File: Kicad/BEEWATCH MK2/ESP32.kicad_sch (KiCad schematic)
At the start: 42 parts, among them J1 USB_C_Receptacle_USB2.0, Q1 DMG6968U, SW1 TK-074-4, SW2 TK-074-4, U1 ESP32-S3FH4R2, Y1 40MHz, Y2 32.768KHz

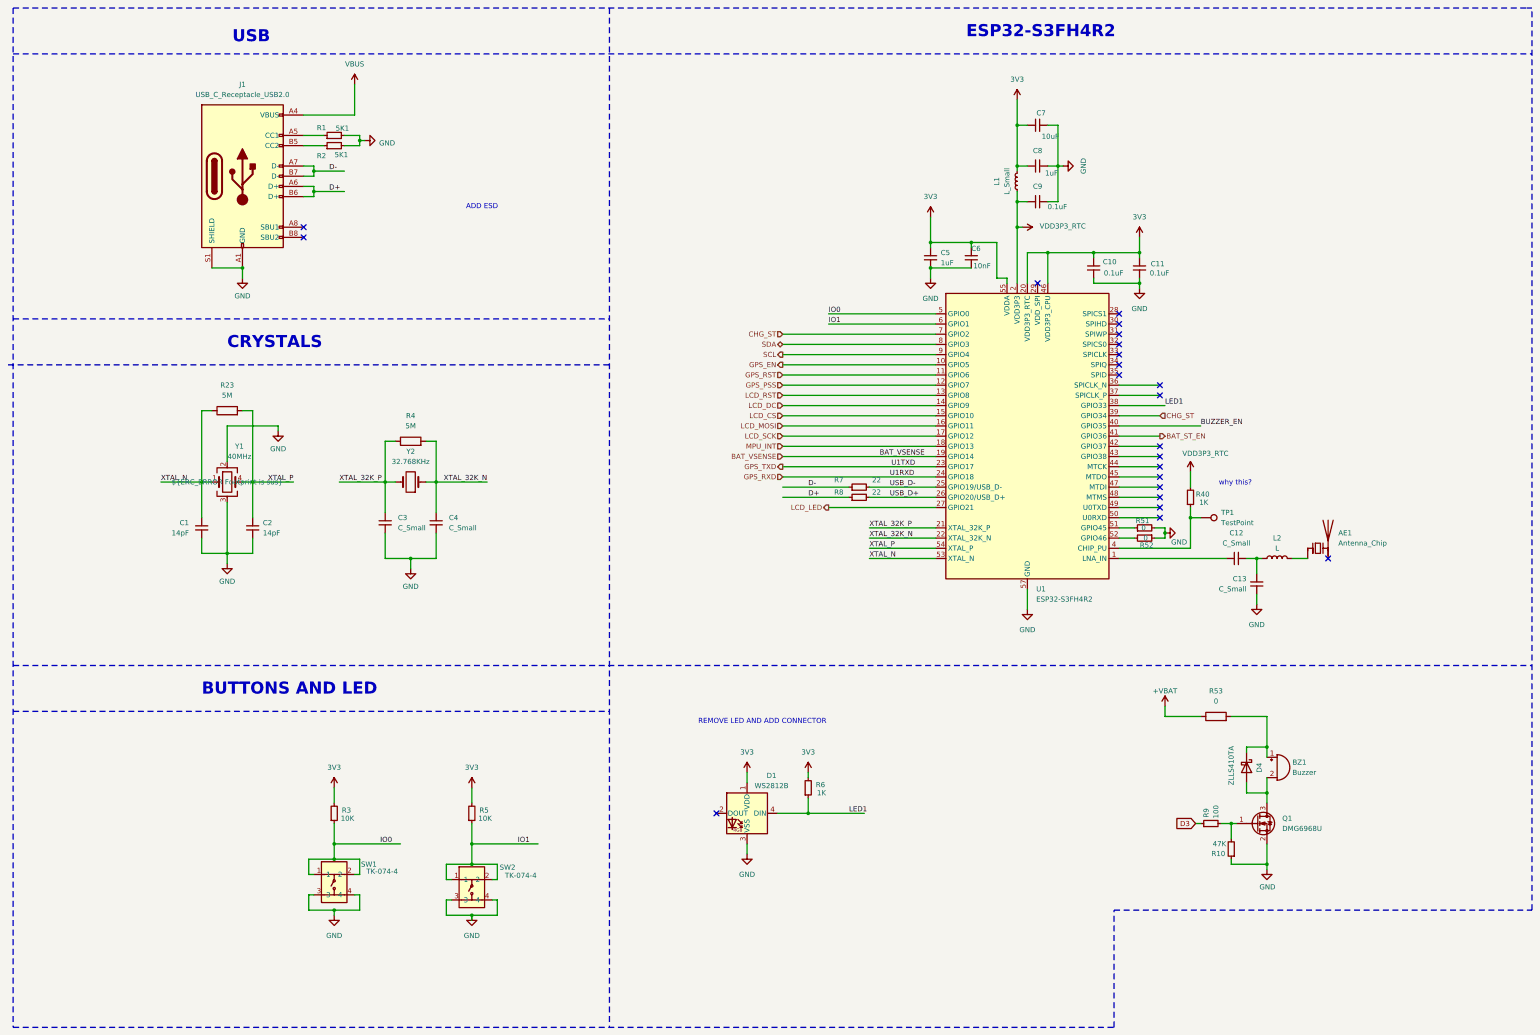
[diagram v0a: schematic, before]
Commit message: ERC going on anf All Lib issue is fixed
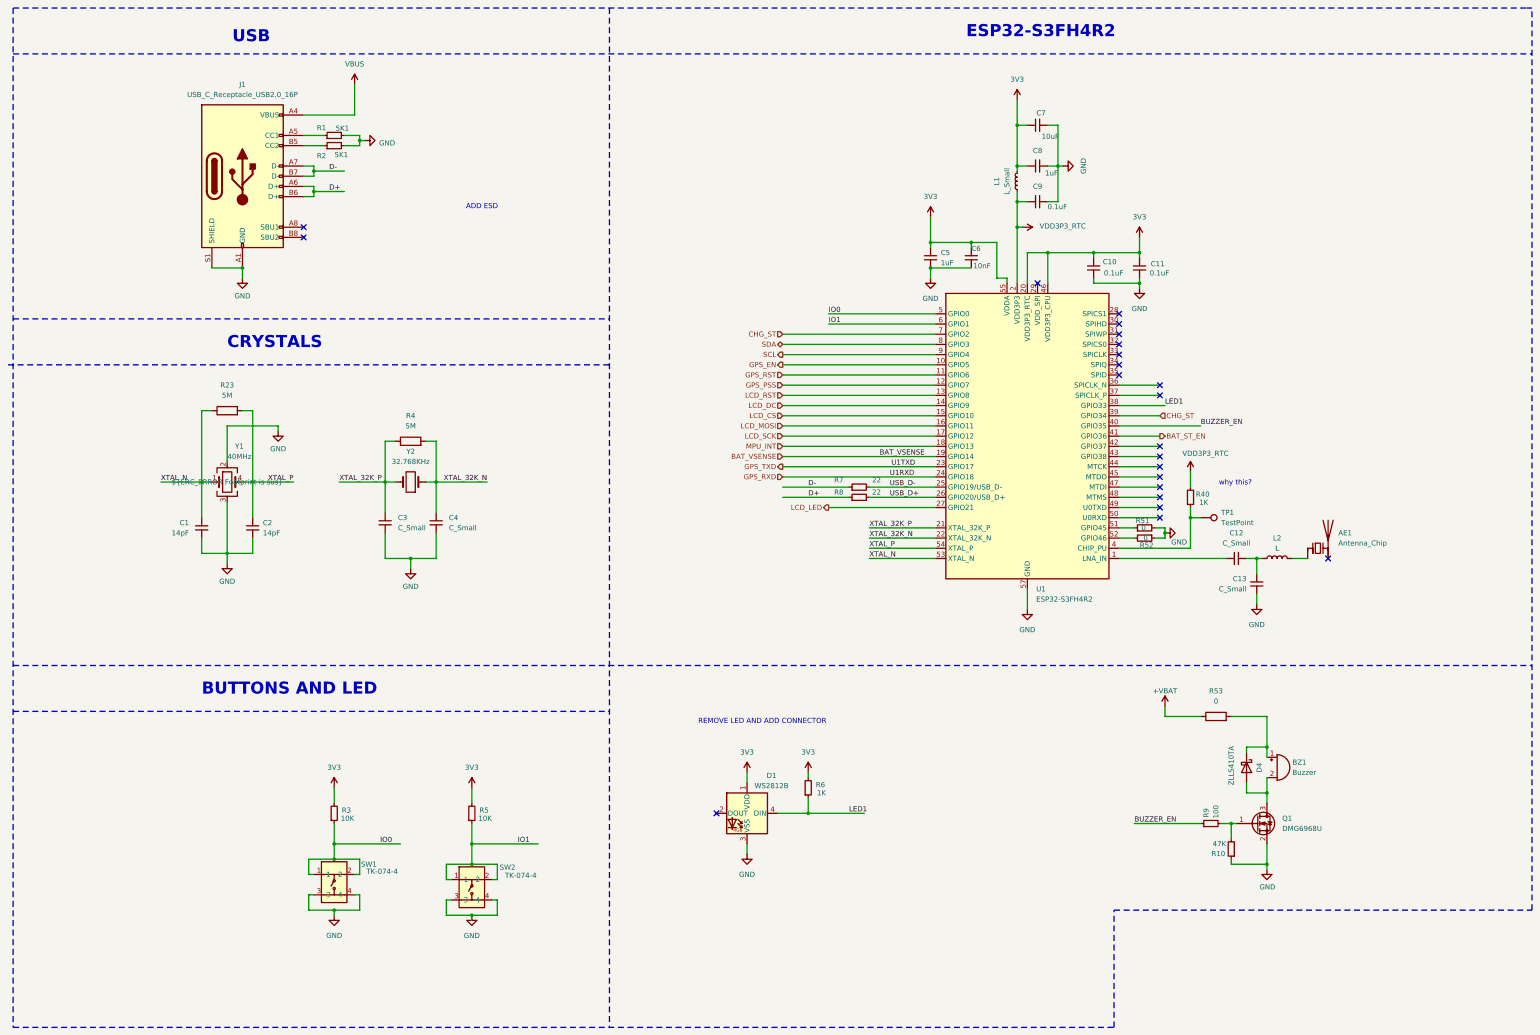
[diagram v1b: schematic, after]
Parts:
- removed J1: USB_C_Receptacle_USB2.0, Connector_USB:USB_C_Receptacle_G-Switch_GT-USB-7010ASV, symbol Connector:USB_C_Receptacle_USB2.0
- added J1: USB_C_Receptacle_USB2.0_16P, symbol Connector:USB_C_Receptacle_USB2.0_16P
- D1: footprint SM_LED:XL-0807RGBC-WS2812B -> LED_SMD:LED_WS2812B_PLCC4_5.0x5.0mm_P3.2mm
- SW1, SW2: footprint SM_SWITCH:Tact Switch-TK-074-4 Pin SMD -> Project:Tact Switch-TK-074-4 Pin SMD
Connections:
- net D3 is gone; now on net BUZZER_EN: R9.1
- net D+: now also J1.A6 (D+), J1.B6 (D+)
- net D-: now also J1.A7 (D-), J1.B7 (D-)
- net GND: now also J1.A1 (GND), J1.A12 (GND), J1.B1 (GND), J1.B12 (GND), J1.S1 (SHIELD)
- net VBUS: now also J1.A4 (VBUS), J1.A9 (VBUS), J1.B4 (VBUS), J1.B9 (VBUS)
- net at R1.1: now also J1.A5 (CC1)
- net at R2.1: now also J1.B5 (CC2)
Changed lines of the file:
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@@
 	)
 	(junction
-		(at 77.47 86.36)
-		(diameter 0)
-		(color 0 0 0 0)
-	)
-	(junction
 		(at 323.85 224.79)
 		(diameter 0)
@@
 	)
 	(junction
+		(at 77.47 86.36)
+		(diameter 0)
+		(color 0 0 0 0)
+	)
+	(junction
 		(at 248.92 86.36)
 		(diameter 0)
@@
 	(wire
 		(pts
-			(xy 314.96 224.79) (xy 316.23 224.79)
+			(xy 299.72 224.79) (xy 316.23 224.79)
 		)
 		(stroke
@@
 		)
 	)
+	(label "BUZZER_EN"
+		(at 299.72 224.79 0)
+		(effects
+			(font
+				(size 1.27 1.27)
+			)
+			(justify left bottom)
+		)
+	)
 	(label "U1TXD"
 		(at 245.11 135.89 180)
@@
 		)
 	)
-	(global_label "D3"
-		(shape input)
-		(at 314.96 224.79 180)
-		(effects
-			(font
-				(size 1.27 1.27)
-			)
-			(justify right)
-		)
-		(property "Intersheetrefs" "${INTERSHEET_REFS}"
-			(at 314.96 224.79 0)
-			(effects
-				(font
-					(size 1.27 1.27)
-				)
-				(hide yes)
-			)
-		)
-	)
 	(hierarchical_label "GPS_RXD"
 		(shape input)
@@
 	)
 	(symbol
-		(lib_id "Connector:USB_C_Receptacle_USB2.0")
-		(at 77.47 63.5 0)
-		(unit 1)
-		(exclude_from_sim no)
-		(in_bom yes)
-		(on_board yes)
-		(dnp no)
-		(fields_autoplaced yes)
-		(property "Reference" "J1"
-			(at 77.47 40.64 0)
-			(effects
-				(font
-					(size 1.27 1.27)
-				)
-			)
-		)
-		(property "Value" "USB_C_Receptacle_USB2.0"
-			(at 77.47 43.18 0)
-			(effects
-				(font
-					(size 1.27 1.27)
-				)
-			)
-		)
-		(property "Footprint" "Connector_USB:USB_C_Receptacle_G-Switch_GT-USB-7010ASV"
-			(at 81.28 63.5 0)
-			(effects
-				(font
-					(size 1.27 1.27)
-				)
-				(hide yes)
-			)
-		)
-		(property "Datasheet" "https://www.usb.org/sites/default/files/documents/usb_type-c.zip"
-			(at 81.28 63.5 0)
-			(effects
-				(font
-					(size 1.27 1.27)
-				)
-				(hide yes)
-			)
-		)
-		(property "Description" ""
-			(at 77.47 63.5 0)
-			(effects
-				(font
-					(size 1.27 1.27)
-				)
-				(hide yes)
-			)
-		)
-		(pin "A1"
-		)
-		(pin "A12"
-		)
-		(pin "A4"
-		)
-		(pin "A5"
-		)
-		(pin "A6"
-		)
-		(pin "A7"
-		)
-		(pin "A8"
-		)
-		(pin "A9"
-		)
-		(pin "B1"
-		)
-		(pin "B12"
-		)
-		(pin "B4"
-		)
-		(pin "B5"
-		)
-		(pin "B6"
-		)
-		(pin "B7"
-		)
-		(pin "B8"
-		)
-		(pin "B9"
-		)
-		(pin "S1"
-		)
-		(instances
-			(project "BEEWATCH"
-				(path "/e9c5fb53-480b-4989-8495-a3341ee99514"
-					(reference "J?")
-					(unit 1)
-				)
-				(path "/e9c5fb53-480b-4989-8495-a3341ee99514/56d77f8e-c069-456f-a514-fdde13f048cd"
-					(reference "J1")
-					(unit 1)
-				)
-			)
-		)
-	)
-	(symbol
 		(lib_id "Transistor_FET:DMG2302U")
 		(at 330.2 224.79 0)
@@
 			)
 		)
-		(property "Footprint" "SM_SWITCH:Tact Switch-TK-074-4 Pin SMD"
+		(property "Footprint" "Project:Tact Switch-TK-074-4 Pin SMD"
 			(at 134.62 233.68 0)
 			(effects
@@
 			)
 		)
-		(property "Footprint" "SM_LED:XL-0807RGBC-WS2812B"
+		(property "Footprint" "LED_SMD:LED_WS2812B_PLCC4_5.0x5.0mm_P3.2mm"
 			(at 201.93 229.87 0)
 			(effects
@@
 			)
 		)
-		(property "Footprint" "SM_SWITCH:Tact Switch-TK-074-4 Pin SMD"
+		(property "Footprint" "Project:Tact Switch-TK-074-4 Pin SMD"
 			(at 100.33 232.41 0)
 			(effects
@@
 					(unit 1)
 				)
+			)
+		)
+	)
+	(symbol
+		(lib_id "Connector:USB_C_Receptacle_USB2.0_16P")
+		(at 77.47 63.5 0)
+		(unit 1)
+		(exclude_from_sim no)
+		(in_bom yes)
+		(on_board yes)
+		(dnp no)
+		(fields_autoplaced yes)
+		(property "Reference" "J1"
+			(at 77.47 40.64 0)
+			(effects
+				(font
+					(size 1.27 1.27)
+				)
+			)
+		)
+		(property "Value" "USB_C_Receptacle_USB2.0_16P"
+			(at 77.47 43.18 0)
+			(effects
+				(font
+					(size 1.27 1.27)
+				)
+			)
+		)
+		(property "Footprint" ""
+			(at 81.28 63.5 0)
+			(effects
+				(font
+					(size 1.27 1.27)
+				)
+				(hide yes)
+			)
+		)
+		(property "Datasheet" "https://www.usb.org/sites/default/files/documents/usb_type-c.zip"
+			(at 81.28 63.5 0)
+			(effects
+				(font
+					(size 1.27 1.27)
+				)
+				(hide yes)
+			)
+		)
+		(property "Description" "USB 2.0-only 16P Type-C Receptacle connector"
+			(at 77.47 63.5 0)
+			(effects
+				(font
+					(size 1.27 1.27)
+				)
+				(hide yes)
+			)
+		)
+		(pin "A8"
+		)
+		(pin "B8"
+		)
+		(pin "B6"
+		)
+		(pin "A6"
+		)
+		(pin "B9"
+		)
+		(pin "B4"
+		)
+		(pin "A5"
+		)
+		(pin "A9"
+		)
+		(pin "A4"
+		)
+		(pin "B12"
+		)
+		(pin "B1"
+		)
+		(pin "A12"
+		)
+		(pin "A1"
+		)
+		(pin "A7"
+		)
+		(pin "B5"
+		)
+		(pin "B7"
+		)
+		(pin "S1"
+		)
+		(instances
+			(project ""
+				(path "/e9c5fb53-480b-4989-8495-a3341ee99514/56d77f8e-c069-456f-a514-fdde13f048cd"
+					(reference "J1")
+					(unit 1)
+				)

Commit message: ERC Checking
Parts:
- removed D1: WS2812B, LED_SMD:LED_WS2812B_PLCC4_5.0x5.0mm_P3.2mm, symbol LED:WS2812B
- J1: footprint (none) -> Connector_USB:USB_C_Receptacle_XKB_U262-16XN-4BVC11
- SW1, SW2: footprint Project:Tact Switch-TK-074-4 Pin SMD -> SM_SWITCH:Tact Switch-TK-074-4 Pin SMD

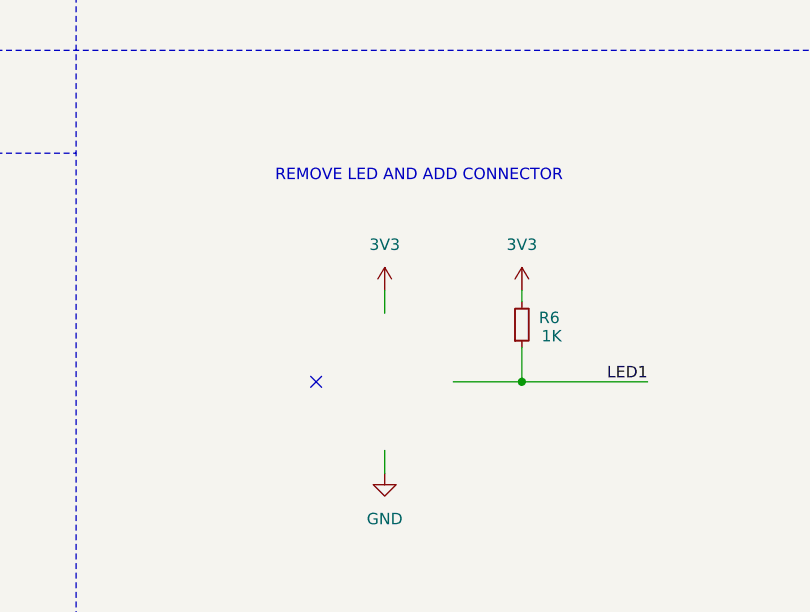
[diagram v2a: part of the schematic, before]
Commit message: Pending task Crystal footprint
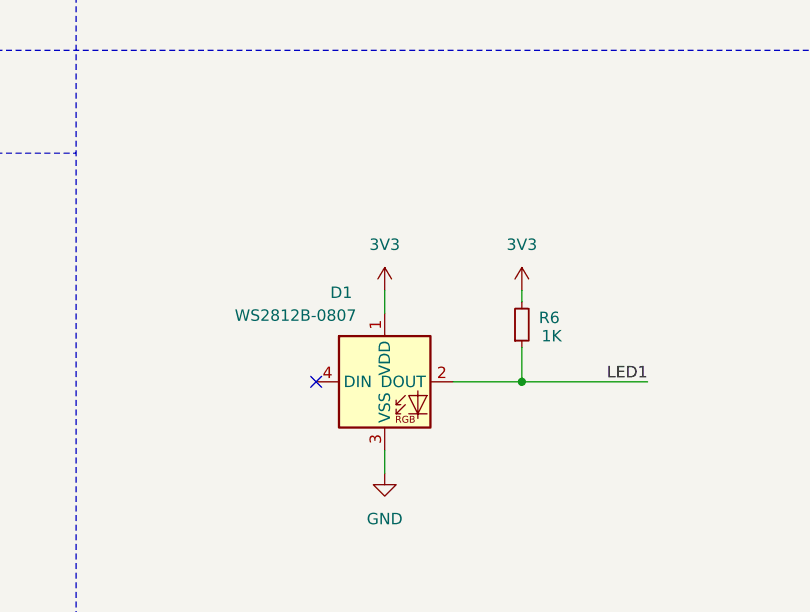
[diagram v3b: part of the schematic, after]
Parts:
- added D1: WS2812B-0807, SM_LED:XL-0807RGBC-WS2812B, symbol SM_LED:WS2812B-0807
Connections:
- net 3V3: now also D1.1 (VDD)
- net GND: now also D1.3 (VSS)
- net LED1: now also D1.2 (DOUT)
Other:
- note removed: "REMOVE LED AND ADD CONNECTOR"
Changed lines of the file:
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@@
 		)
 	)
-	(text "REMOVE LED AND ADD CONNECTOR\n"
-		(exclude_from_sim no)
-		(at 207.01 199.39 0)
-		(effects
-			(font
-				(size 1.27 1.27)
-			)
-		)
-	)
 	(text "ADD ESD\n"
 		(exclude_from_sim no)
@@
 					(unit 1)
 				)
+			)
+		)
+	)
+	(symbol
+		(lib_id "SM_LED:WS2812B-0807")
+		(at 195.58 222.25 0)
+		(unit 1)
+		(exclude_from_sim no)
+		(in_bom yes)
+		(on_board yes)
+		(dnp no)
+		(property "Reference" "D1"
+			(at 198.374 212.344 0)
+			(effects
+				(font
+					(size 1.27 1.27)
+				)
+			)
+		)
+		(property "Value" "WS2812B-0807"
+			(at 193.294 214.884 0)
+			(effects
+				(font
+					(size 1.27 1.27)
+				)
+			)
+		)
+		(property "Footprint" "SM_LED:XL-0807RGBC-WS2812B"
+			(at 227.076 219.71 0)
+			(effects
+				(font
+					(size 1.27 1.27)
+				)
+				(hide yes)
+			)
+		)
+		(property "Datasheet" ""
+			(at 195.58 222.25 0)
+			(effects
+				(font
+					(size 1.27 1.27)
+				)
+				(hide yes)
+			)
+		)
+		(property "Description" ""
+			(at 195.58 222.25 0)
+			(effects
+				(font
+					(size 1.27 1.27)
+				)
+				(hide yes)
+			)
+		)
+		(pin "2"
+		)
+		(pin "1"
+		)
+		(pin "4"
+		)
+		(pin "3"
+		)
+		(instances
+			(project ""
+				(path "/e9c5fb53-480b-4989-8495-a3341ee99514/56d77f8e-c069-456f-a514-fdde13f048cd"
+					(reference "D1")
+					(unit 1)
+				)

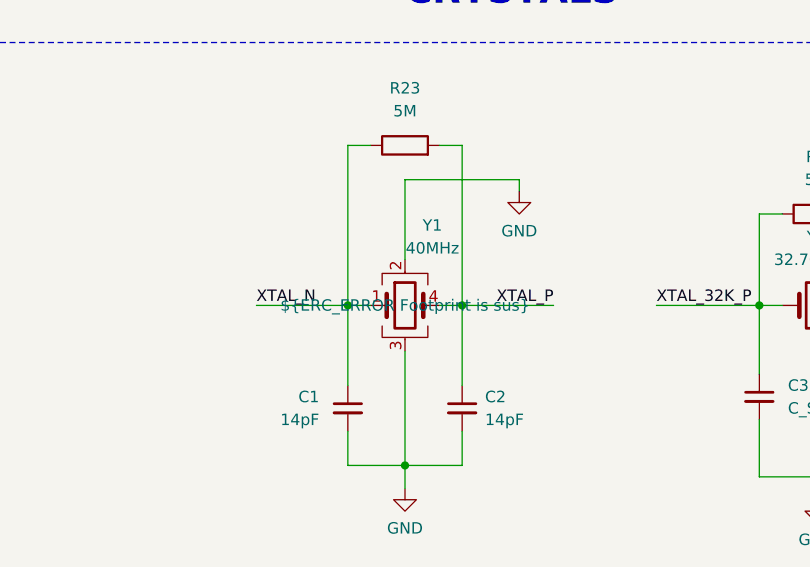
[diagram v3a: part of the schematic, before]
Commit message: Crystal footprint fixed
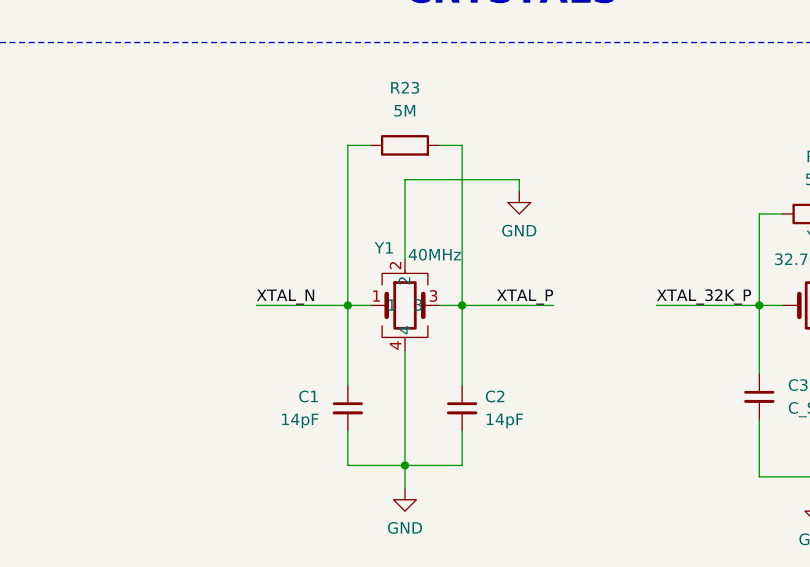
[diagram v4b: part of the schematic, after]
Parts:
- removed Y1: 40MHz, Crystal:Crystal_SMD_2016-4Pin_2.0x1.6mm, symbol Device:Crystal_GND23
- added Y1: 40MHz, Crystal:Crystal_SMD_2016-4Pin_2.0x1.6mm, symbol SM_CRYSTAL:2x3
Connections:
- net GND: now also Y1.2, Y1.4
- net XTAL_N: now also Y1.1
- net XTAL_P: now also Y1.3
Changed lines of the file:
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@@
 	)
 	(symbol
+		(lib_id "SM_CRYSTAL:2x3")
+		(at 73.66 134.62 0)
+		(unit 1)
+		(exclude_from_sim no)
+		(in_bom yes)
+		(on_board yes)
+		(dnp no)
+		(property "Reference" "Y1"
+			(at 71.374 133.35 0)
+			(effects
+				(font
+					(size 1.27 1.27)
+				)
+			)
+		)
+		(property "Value" "40MHz"
+			(at 76.962 134.112 0)
+			(effects
+				(font
+					(size 1.27 1.27)
+				)
+			)
+		)
+		(property "Footprint" "Crystal:Crystal_SMD_2016-4Pin_2.0x1.6mm"
+			(at 73.66 134.62 0)
+			(effects
+				(font
+					(size 1.27 1.27)
+				)
+				(hide yes)
+			)
+		)
+		(property "Datasheet" ""
+			(at 73.66 134.62 0)
+			(effects
+				(font
+					(size 1.27 1.27)
+				)
+				(hide yes)
+			)
+		)
+		(property "Description" ""
+			(at 73.66 134.62 0)
+			(effects
+				(font
+					(size 1.27 1.27)
+				)
+				(hide yes)
+			)
+		)
+		(pin "3"
+		)
+		(pin "1"
+		)
+		(pin "2"
+		)
+		(pin "4"
+		)
+		(instances
+			(project ""
+				(path "/e9c5fb53-480b-4989-8495-a3341ee99514/56d77f8e-c069-456f-a514-fdde13f048cd"
+					(reference "Y1")
+					(unit 1)
+				)
+			)
+		)
+	)
+	(symbol
 		(lib_id "Transistor_FET:DMG2302U")
 		(at 330.2 224.79 0)
@@
 					(unit 1)
 				)
-			)
-		)
-	)
-	(symbol
-		(lib_id "Device:Crystal_GND23")
-		(at 73.66 139.7 0)
-		(unit 1)
-		(exclude_from_sim no)
-		(in_bom yes)
-		(on_board yes)
-		(dnp no)
-		(property "Reference" "Y1"
-			(at 76.708 130.81 0)
-			(effects
-				(font
-					(size 1.27 1.27)
-				)
-			)
-		)
-		(property "Value" "40MHz"
-			(at 76.708 133.35 0)
-			(effects
-				(font
-					(size 1.27 1.27)
-				)
-			)
-		)
-		(property "Footprint" "Crystal:Crystal_SMD_2016-4Pin_2.0x1.6mm"
-			(at 73.66 139.7 0)
-			(effects
-				(font
-					(size 1.27 1.27)
-				)
-				(hide yes)
-			)
-		)
-		(property "Datasheet" "~"
-			(at 73.66 139.7 0)
-			(effects
-				(font
-					(size 1.27 1.27)
-				)
-				(hide yes)
-			)
-		)
-		(property "Description" "Four pin crystal, GND on pins 2 and 3"
-			(at 73.66 139.7 0)
-			(effects
-				(font
-					(size 1.27 1.27)
-				)
-				(hide yes)
-			)
-		)
-		(property "TODO" "${ERC_ERROR Footprint is sus}"
-			(at 73.66 139.7 0)
-			(effects
-				(font
-					(size 1.27 1.27)
-				)
-			)
-		)
-		(pin "3"
-		)
-		(pin "1"
-		)
-		(pin "4"
-		)
-		(pin "2"
-		)
-		(instances
-			(project ""
-				(path "/e9c5fb53-480b-4989-8495-a3341ee99514/56d77f8e-c069-456f-a514-fdde13f048cd"
-					(reference "Y1")
-					(unit 1)
-				)

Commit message: Deep optmization 90% completed
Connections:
- net 3V3 renamed +3.3V

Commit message: Duplicate pin changed
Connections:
- net BUZZER_EN: now also U1.7 (GPIO2); no longer U1.40 (GPIO35)
- net CHG_ST: no longer U1.7 (GPIO2)
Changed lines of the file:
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@@
+	(wire
+		(pts
+			(xy 250.19 102.87) (xy 229.87 102.87)
+		)
+		(stroke
+			(width 0)
+			(type default)
+		)
+	)
 	(wire
 		(pts
@@
 	(wire
 		(pts
-			(xy 295.91 125.73) (xy 316.23 125.73)
-		)
-		(stroke
-			(width 0)
-			(type default)
-		)
-	)
-	(wire
-		(pts
 			(xy 330.2 158.75) (xy 330.2 162.56)
 		)
@@
 		(pts
 			(xy 105.41 242.57) (xy 106.68 242.57)
-		)
-		(stroke
-			(width 0)
-			(type default)
-		)
-	)
-	(wire
-		(pts
-			(xy 212.09 102.87) (xy 250.19 102.87)
 		)
 		(stroke
@@
 		)
 	)
+	(label "BUZZER_EN"
+		(at 229.87 102.87 180)
+		(effects
+			(font
+				(size 1.27 1.27)
+			)
+			(justify right bottom)
+		)
+	)
 	(label "IO1"
 		(at 151.13 229.87 180)
@@
 	(label "LED1"
 		(at 307.34 120.65 0)
-		(effects
-			(font
-				(size 1.27 1.27)
-			)
-			(justify left bottom)
-		)
-	)
-	(label "BUZZER_EN"
-		(at 316.23 125.73 0)
 		(effects
 			(font
@@
 		(effects
 			(font
-				(size 1.27 1.27)
-			)
-			(justify right)
-		)
-	)
-	(hierarchical_label "CHG_ST"
-		(shape input)
-		(at 212.09 102.87 180)
-		(effects
-			(font
